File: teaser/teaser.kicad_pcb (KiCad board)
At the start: 2 copper layers, 43 x 115 mm, 72 parts, among them J1 Programator, J2 AC_Plug, J3 OLED, J4 battery, Q1 MMBTA44, Q2 MMBTA44, Q3 MMBTA44, Q4 MMBTA44, Q6 AO3401A, SW1 Włancznik, SW2 SW_SPST, SW3 Manual, SW4 Manual, SW5 Manual, SW7 SW_Push, U2 LM1117MP-5.0, U3 ATmega328P-A, Y1 16kHz

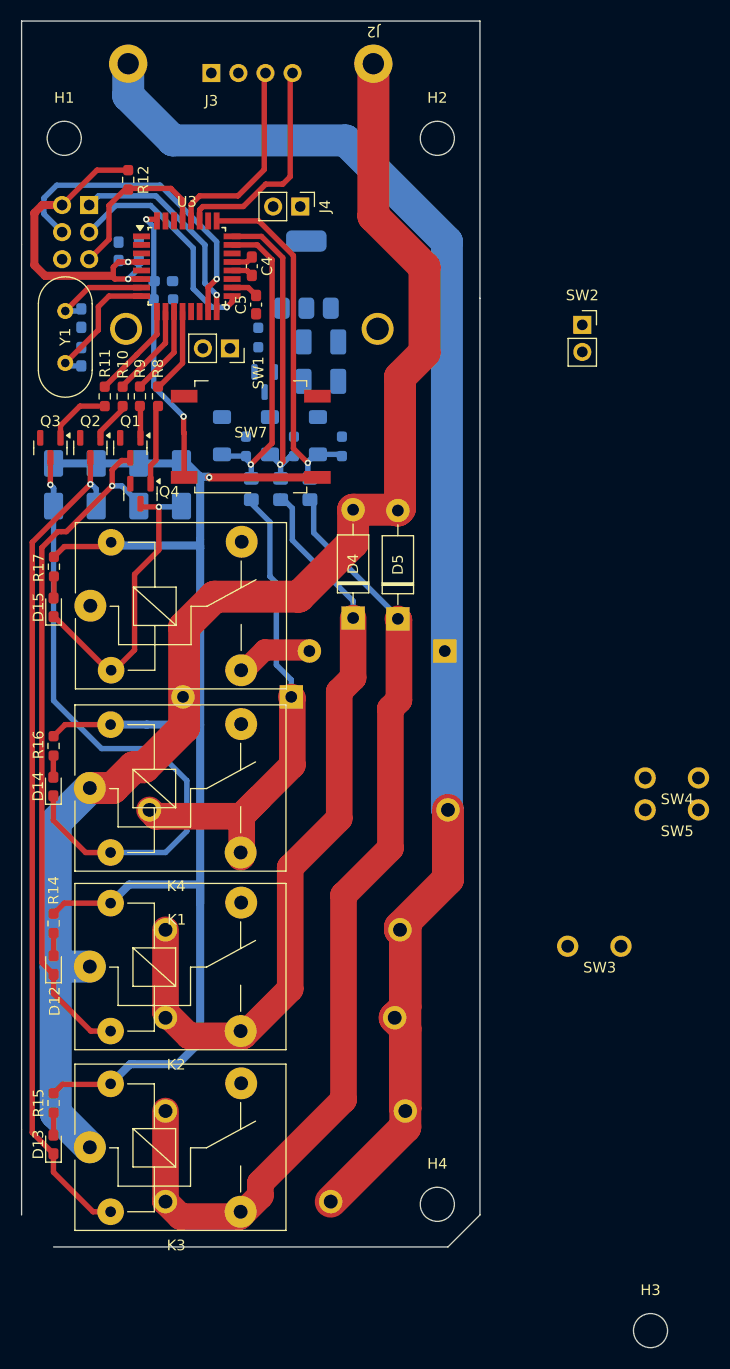
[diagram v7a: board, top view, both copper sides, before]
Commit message: Layout finished, tracks routed, only silkscreen left
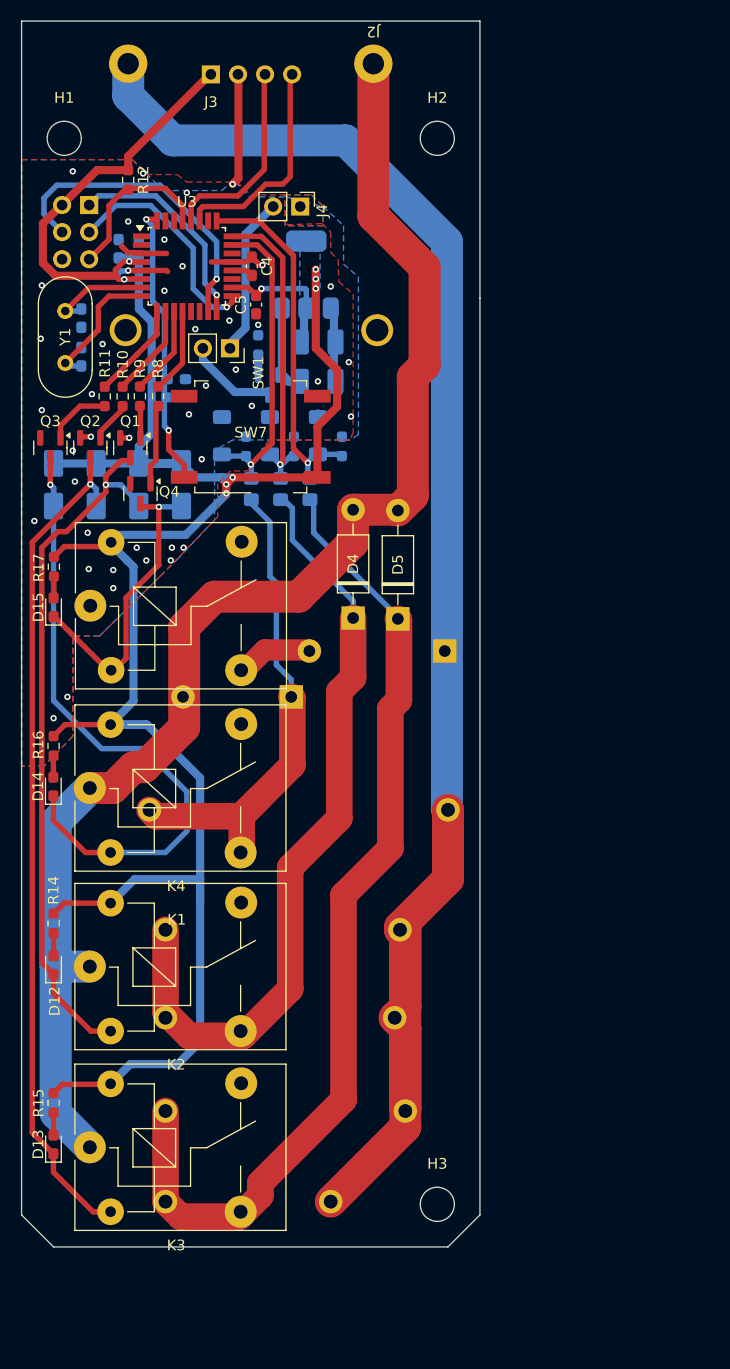
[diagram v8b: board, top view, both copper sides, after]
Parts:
- removed H4: MountingHole, MountingHole:MountingHole_3.2mm_M3_DIN965
- removed SW2: SW_SPST, Connector_PinSocket_2.54mm:PinSocket_1x02_P2.54mm_Vertical
- removed SW3, SW4, SW5: Manual, Teaser:230V_switch
- moved H3 23.2 mm to (90.0, 177.0)
- moved R7 9.28 mm to (65.5, 101.3)
- moved C9 9.28 mm to (65.5, 99.6)
- moved R13 0.70 mm to (73.2, 96.4)
- moved Q6 0.45 mm to (74.2, 100.1)
- moved C1 0.25 mm to (78.8, 99.8)
- moved C2 0.25 mm to (78.8, 96.1)
- moved C3 0.24 mm to (62.0, 87.4)
- moved C6 0.24 mm to (60.1, 87.4)
- moved J3 0.13 mm to (68.8, 71.0)
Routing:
- net VCC: track 174.5 -> 247.7 mm, vias 3 -> 9
- net GND: track 2.04 -> 37.2 mm, vias 0 -> 43
- net Net-(J4-Pin_2): track 0.00 -> 15.0 mm
- net Net-(Q6-S): track 0.00 -> 11.0 mm
- net Net-(Q6-D): track 0.00 -> 8.14 mm
- net Net-(Q6-G): track 0.00 -> 1.90 mm
- net Net-(D12-K): track 65.1 -> 65.8 mm
- net Net-(D14-K): track 61.7 -> 61.0 mm
- added copper zone on B.Cu, net GND
- added copper zone on F.Cu, net GND
- added copper zone on B.Cu, net VCC
